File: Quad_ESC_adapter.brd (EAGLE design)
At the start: 96.5 x 40.1 mm, 28 parts, among them Y1 ECS-80-S-4X

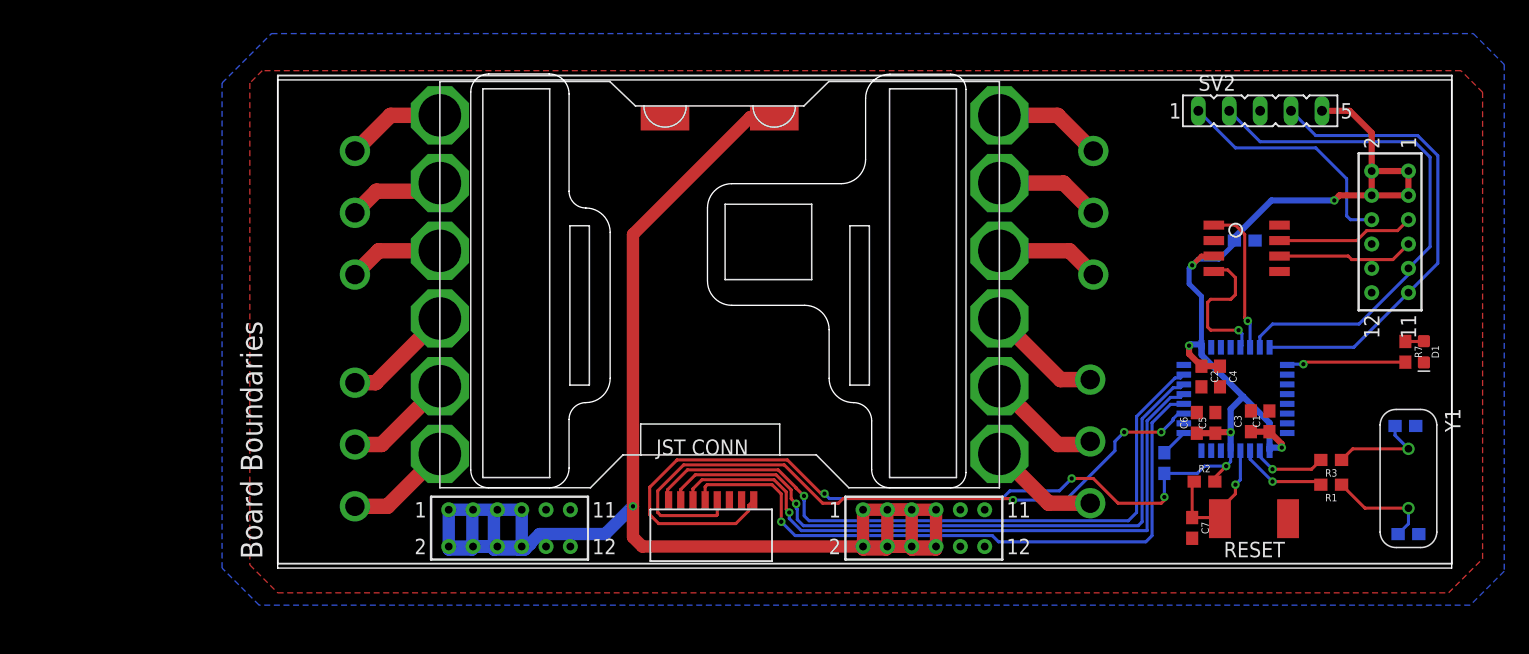
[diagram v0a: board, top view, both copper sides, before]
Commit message: split into adapter board
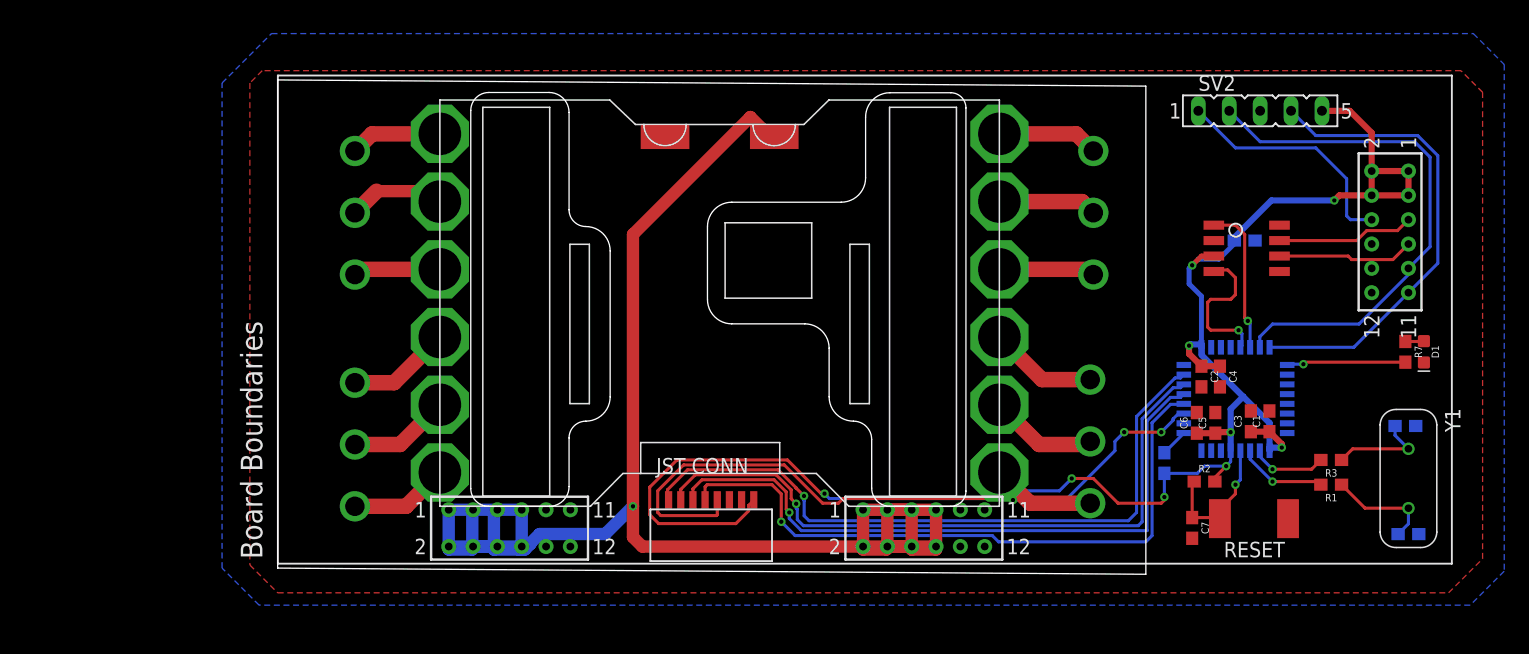
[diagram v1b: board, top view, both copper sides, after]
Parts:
- moved U$10 1.52 mm to (13.3, 5.08)
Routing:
- net ESC4_B: track 9.55 -> 8.92 mm
- net ESC2_B: track 9.17 -> 8.54 mm
- net ESC3_R: track 8.53 -> 7.90 mm
- net ESC2_Y: track 8.97 -> 8.34 mm
- net ESC1_R: track 7.79 -> 7.16 mm
- net ESC4_R: track 9.14 -> 8.51 mm
- net ESC3_Y: track 8.73 -> 8.10 mm
- net ESC2_R: track 8.77 -> 8.14 mm
- net +12V: track 139.0 -> 139.6 mm
- net ESC4_Y: track 9.56 -> 8.93 mm
- net ESC3_B: track 8.94 -> 8.31 mm
- net ESC1_B: track 8.20 -> 7.57 mm
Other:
- board size 96.5 x 40.1 mm -> 71.4 x 40.6 mm
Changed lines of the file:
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@@
 <board>
 <plain>
-<wire x1="0" y1="0" x2="96.52" y2="0" width="0" layer="20"/>
-<wire x1="96.52" y1="0" x2="96.52" y2="40.132" width="0" layer="20"/>
-<wire x1="96.52" y1="40.132" x2="0" y2="40.132" width="0" layer="20"/>
+<wire x1="0" y1="0" x2="71.374" y2="-0.508" width="0" layer="20"/>
+<wire x1="71.374" y1="-0.508" x2="71.374" y2="39.624" width="0" layer="20"/>
+<wire x1="71.374" y1="39.624" x2="0" y2="40.132" width="0" layer="20"/>
 <wire x1="0" y1="40.132" x2="0" y2="0" width="0" layer="20"/>
 </plain>
@@
 <attribute name="VALUE" x="79.44111875" y="25.97543125" size="1.27245" layer="27" rot="R180"/>
 </element>
-<element name="U$10" library="BLHeli_32 45A" package="LUMENIER_QUAD" package3d_urn="urn:adsk.eagle:package:24294694/3" value="LUMENIER_QUAD" x="13.335" y="6.604" smashed="yes"/>
+<element name="U$10" library="BLHeli_32 45A" package="LUMENIER_QUAD" package3d_urn="urn:adsk.eagle:package:24294694/3" value="LUMENIER_QUAD" x="13.335" y="5.08" smashed="yes"/>
 <element name="R4" library="SparkFun-Resistors" library_urn="urn:adsk.eagle:library:532" package="0603" package3d_urn="urn:adsk.eagle:package:39650/1" value="10k" x="72.898" y="8.636" smashed="yes" rot="MR90">
 <attribute name="NAME" x="73.66" y="8.636" size="0.6096" layer="26" font="vector" ratio="20" rot="MR90" align="bottom-center"/>
@@
 <wire x1="52.1244" y1="1.7738" x2="54.1244" y2="1.7738" width="1.016" layer="1"/>
 <wire x1="50.1244" y1="1.7738" x2="52.1244" y2="1.7738" width="1.016" layer="1"/>
-<wire x1="38.862" y1="37.084" x2="38.972" y2="36.974" width="1.016" layer="1"/>
+<wire x1="38.862" y1="37.084" x2="40.496" y2="35.45" width="1.016" layer="1"/>
 <wire x1="38.862" y1="37.084" x2="29.21" y2="27.432" width="1.016" layer="1"/>
-<wire x1="38.972" y1="36.974" x2="40.825" y2="36.974" width="1.016" layer="1"/>
+<wire x1="40.496" y1="35.45" x2="40.825" y2="35.45" width="1.016" layer="1"/>
 <wire x1="50.1244" y1="1.7738" x2="51.8746" y2="1.7738" width="1.016" layer="1"/>
 <wire x1="51.8746" y1="1.7738" x2="52.1244" y2="1.524" width="1.016" layer="1"/>
@@
 <contactref element="U$7" pad="A"/>
 <contactref element="U$10" pad="9"/>
-<wire x1="59.335" y1="20.524" x2="64.365" y2="15.494" width="1.27" layer="1"/>
-<wire x1="64.365" y1="15.494" x2="66.802" y2="15.494" width="1.27" layer="1"/>
+<wire x1="59.335" y1="19" x2="62.841" y2="15.494" width="1.27" layer="1"/>
+<wire x1="62.841" y1="15.494" x2="66.802" y2="15.494" width="1.27" layer="1"/>
 </signal>
 <signal name="ESC4_Y">
 <contactref element="U$7" pad="B"/>
 <contactref element="U$10" pad="8"/>
-<wire x1="59.335" y1="14.954" x2="64.129" y2="10.16" width="1.27" layer="1"/>
-<wire x1="66.294" y1="10.16" x2="64.129" y2="10.16" width="1.27" layer="1"/>
+<wire x1="59.335" y1="13.43" x2="62.605" y2="10.16" width="1.27" layer="1"/>
+<wire x1="66.294" y1="10.16" x2="62.605" y2="10.16" width="1.27" layer="1"/>
 <wire x1="66.802" y1="10.414" x2="66.548" y2="10.16" width="1.016" layer="1"/>
 <wire x1="66.548" y1="10.16" x2="66.294" y2="10.16" width="1.016" layer="1"/>
@@
 <contactref element="U$7" pad="C"/>
 <contactref element="U$10" pad="7"/>
-<wire x1="59.335" y1="9.384" x2="63.385" y2="5.334" width="1.27" layer="1"/>
-<wire x1="63.385" y1="5.334" x2="66.802" y2="5.334" width="1.27" layer="1"/>
+<wire x1="59.335" y1="7.86" x2="61.861" y2="5.334" width="1.27" layer="1"/>
+<wire x1="61.861" y1="5.334" x2="66.802" y2="5.334" width="1.27" layer="1"/>
 </signal>
 <signal name="ESC3_B">
 <contactref element="U$6" pad="A"/>
 <contactref element="U$10" pad="12"/>
-<wire x1="67.056" y1="34.29" x2="64.122" y2="37.224" width="1.27" layer="1"/>
-<wire x1="64.122" y1="37.224" x2="59.335" y2="37.224" width="1.27" layer="1"/>
+<wire x1="67.056" y1="34.29" x2="65.646" y2="35.7" width="1.27" layer="1"/>
+<wire x1="65.646" y1="35.7" x2="59.335" y2="35.7" width="1.27" layer="1"/>
 </signal>
 <signal name="ESC3_Y">
 <contactref element="U$6" pad="B"/>
 <contactref element="U$10" pad="11"/>
-<wire x1="59.335" y1="31.654" x2="64.612" y2="31.654" width="1.27" layer="1"/>
-<wire x1="64.612" y1="31.654" x2="67.056" y2="29.21" width="1.27" layer="1"/>
+<wire x1="59.335" y1="30.13" x2="66.136" y2="30.13" width="1.27" layer="1"/>
+<wire x1="66.136" y1="30.13" x2="67.056" y2="29.21" width="1.27" layer="1"/>
 </signal>
 <signal name="ESC3_R">
 <contactref element="U$6" pad="C"/>
 <contactref element="U$10" pad="10"/>
-<wire x1="59.335" y1="26.084" x2="65.102" y2="26.084" width="1.27" layer="1"/>
-<wire x1="65.102" y1="26.084" x2="67.056" y2="24.13" width="1.27" layer="1"/>
+<wire x1="59.335" y1="24.56" x2="66.626" y2="24.56" width="1.27" layer="1"/>
+<wire x1="66.626" y1="24.56" x2="67.056" y2="24.13" width="1.27" layer="1"/>
 </signal>
 <signal name="ESC2_B">
 <contactref element="U$5" pad="A"/>
 <contactref element="U$10" pad="4"/>
-<wire x1="13.335" y1="20.524" x2="8.051" y2="15.24" width="1.27" layer="1"/>
-<wire x1="8.051" y1="15.24" x2="6.35" y2="15.24" width="1.27" layer="1"/>
+<wire x1="13.335" y1="19" x2="9.575" y2="15.24" width="1.27" layer="1"/>
+<wire x1="9.575" y1="15.24" x2="6.35" y2="15.24" width="1.27" layer="1"/>
 </signal>
 <signal name="ESC2_Y">
 <contactref element="U$5" pad="B"/>
 <contactref element="U$10" pad="5"/>
-<wire x1="13.335" y1="14.954" x2="8.541" y2="10.16" width="1.27" layer="1"/>
-<wire x1="8.541" y1="10.16" x2="6.35" y2="10.16" width="1.27" layer="1"/>
+<wire x1="13.335" y1="13.43" x2="10.065" y2="10.16" width="1.27" layer="1"/>
+<wire x1="10.065" y1="10.16" x2="6.35" y2="10.16" width="1.27" layer="1"/>
 </signal>
 <signal name="ESC2_R">
 <contactref element="U$5" pad="C"/>
 <contactref element="U$10" pad="6"/>
-<wire x1="13.335" y1="9.384" x2="9.031" y2="5.08" width="1.27" layer="1"/>
-<wire x1="9.031" y1="5.08" x2="6.35" y2="5.08" width="1.27" layer="1"/>
+<wire x1="13.335" y1="7.86" x2="10.555" y2="5.08" width="1.27" layer="1"/>
+<wire x1="10.555" y1="5.08" x2="6.35" y2="5.08" width="1.27" layer="1"/>
 </signal>
 <signal name="ESC1_B">
 <contactref element="U$1" pad="A"/>
 <contactref element="U$10" pad="1"/>
-<wire x1="6.35" y1="34.29" x2="9.284" y2="37.224" width="1.27" layer="1"/>
-<wire x1="9.284" y1="37.224" x2="13.335" y2="37.224" width="1.27" layer="1"/>
+<wire x1="6.35" y1="34.29" x2="7.76" y2="35.7" width="1.27" layer="1"/>
+<wire x1="7.76" y1="35.7" x2="13.335" y2="35.7" width="1.27" layer="1"/>
 </signal>
 <signal name="ESC1_Y">
@@
 <contactref element="U$10" pad="2"/>
 <wire x1="6.35" y1="29.21" x2="8.128" y2="30.988" width="1.27" layer="1"/>
-<wire x1="12.954" y1="30.988" x2="8.128" y2="30.988" width="1.27" layer="1"/>
-<wire x1="13.335" y1="31.654" x2="12.954" y2="31.273" width="1.016" layer="1"/>
-<wire x1="12.954" y1="31.273" x2="12.954" y2="30.988" width="1.016" layer="1"/>
+<wire x1="13.335" y1="30.13" x2="12.477" y2="30.988" width="1.016" layer="1"/>
+<wire x1="12.477" y1="30.988" x2="8.128" y2="30.988" width="1.016" layer="1"/>
 </signal>
 <signal name="ESC1_R">
 <contactref element="U$1" pad="C"/>
 <contactref element="U$10" pad="3"/>
-<wire x1="6.35" y1="24.13" x2="8.304" y2="26.084" width="1.27" layer="1"/>
-<wire x1="8.304" y1="26.084" x2="13.335" y2="26.084" width="1.27" layer="1"/>
+<wire x1="6.35" y1="24.13" x2="6.78" y2="24.56" width="1.27" layer="1"/>
+<wire x1="6.78" y1="24.56" x2="13.335" y2="24.56" width="1.27" layer="1"/>
 </signal>
 <signal name="CAN_H">

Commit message: complete connector placement
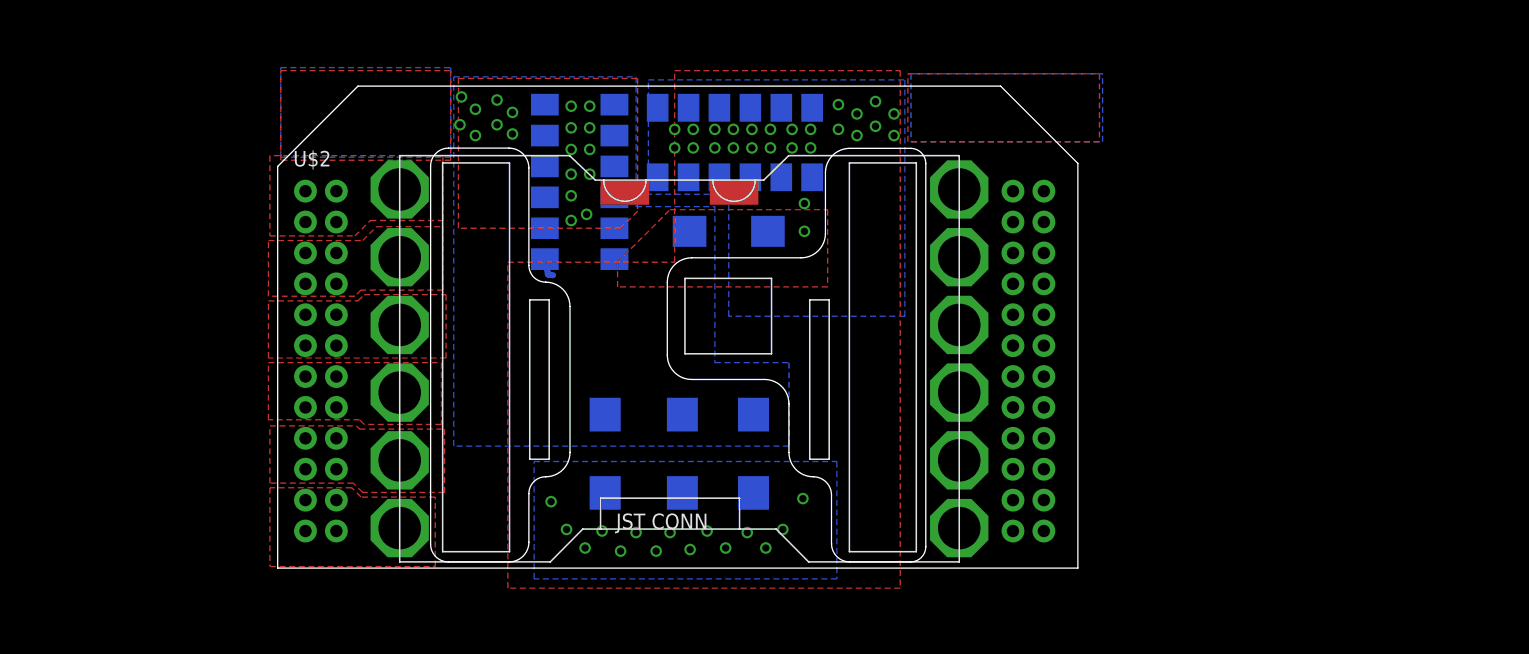
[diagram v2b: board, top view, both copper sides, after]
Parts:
- removed C10: 100nF, SparkFun-Capacitors:0603
- removed C5, C6, C7, C8, C9: 4.7uF, SparkFun-Capacitors:0603
- removed D1: (no value), SparkFun-LED:LED-0603
- removed R1, R2, R3: 1k, SparkFun-Resistors:0603
- removed R4: 10k, SparkFun-Resistors:0603
- removed R7: (no value), SparkFun-Resistors:0603
- removed RESET: (no value), DiscreteComponents:SW_2512
- removed SV2: (no value), con-lsta:FE05-1
- removed U$1, U$5, U$6, U$7: 3PINCONNECTOR, BLHeli_32 45A:3PINCONNECTOR
- removed U$3: BACKPLANE_CONNECTORS, BLHeli_32 45A:BACKPLANE_CONNECTORS
- removed U$4: STM32F042K6T6, PI_Shield_Library:STM32F042K6T6
- removed U$8: TCAN337D, PI_Shield_Library:TCAN337D
- removed Y1: ECS-80-S-4X, ECS-80-S-4X:XTAL_ECS-80-S-4X
- C1, C2, C3, C4: value 4.7uF -> 150uF; device SparkFun-Capacitors:0603 -> Tantalum Cap 150 uF - Kemet 2917 T491:2917(7343-31-METRIC)
- U$2: value 8PIN_CONNECTOR -> BACKPLANE_ESC_ADAPTER_ESC; device BLHeli_32 45A:8PI_CONNECTOR -> Backplane_ESC_adapter:BACKPLANE_ESC_ADAPTER_ESC
- moved C1 54.7 mm to (26.9, 9.40), flipped to the bottom
- moved C2 43.1 mm to (33.3, 9.40), flipped to the bottom, turned to 90 degrees
- moved C4 42.1 mm to (37.1, 27.7), flipped to the bottom, turned to 0 degrees
- moved C3 41.0 mm to (39.1, 9.40), flipped to the bottom
- moved U$2 40.9 mm to (0.00, 0.00), turned to 0 degrees
- moved U$10 5.64 mm to (10.0, 0.51)
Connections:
- removed net +12V: U$10.VIN, U$3.1, U$3.13, U$3.14, U$3.15, U$3.16, U$3.17, U$3.18, U$3.19, U$3.2, U$3.20, U$3.3, U$3.4, U$3.5, U$3.6, U$3.7, U$3.8
- removed net +3V3: C1.1, C10.1, C2.1, C3.1, C4.1, C5.1, C6.1, R2.2, R4.1, SV2.5, U$2.P$1, U$3.25, U$3.26, U$3.27, U$3.28, U$4.VDD, U$4.VDDA, U$4.VDDIO2, U$8.VCC
- removed net CAN_H: U$3.29, U$8.CANH
- removed net CAN_L: U$3.31, U$8.CANL
- removed net CAN_RX: U$4.PA11, U$8.RXD
- removed net CAN_TX: U$4.PA12, U$8.TXD
- removed net LED: R7.2, U$4.PA15
- removed net N$1: C9.1, R1.1, Y1.2
- removed net N$2: C8.1, R3.1, Y1.1
- removed net N$24: D1.A, R7.1
- removed net N$3: R4.2, U$4.PA3
- removed net N$7: U$3.32
- removed net N$8: U$3.36
- removed net NRST: SV2.1, U$3.30
- removed net NRST1: C7.1, R2.1, RESET.2, U$4.NRST
- removed net OSC_IN: R3.2, U$4.PF0-OSC_IN
- removed net OSC_OUT: R1.2, U$4.PF1-OSC_OUT
- removed net SWCLK: SV2.4, U$3.35, U$4.PA14
- removed net SWDIO: SV2.2, U$3.33, U$4.PA13
- removed net TIM3_CH1: U$2.P$5, U$4.PA6
- removed net TIM3_CH2: U$2.P$6, U$4.PA7
- removed net TIM3_CH3: U$2.P$7, U$4.PB0
- removed net TIM3_CH4: U$2.P$8, U$4.PB1
- removed net TLM: U$2.P$4, U$4.PA5
- new net 12V: C1.+, C2.+, C3.+, C4.+, U$10.VIN, U$2.12V@1, U$2.12V@10, U$2.12V@11, U$2.12V@12, U$2.12V@2, U$2.12V@3, U$2.12V@4, U$2.12V@5, U$2.12V@6, U$2.12V@7, U$2.12V@8, U$2.12V@9
- net ESC1_B: now also U$2.ESC1_P1@1, U$2.ESC1_P1@2, U$2.ESC1_P1@3, U$2.ESC1_P1@4; no longer U$1.A
- net ESC1_R: now also U$2.ESC1_P3@1, U$2.ESC1_P3@2, U$2.ESC1_P3@3, U$2.ESC1_P3@4; no longer U$1.C
- net ESC1_Y: now also U$2.ESC1_P2@1, U$2.ESC1_P2@2, U$2.ESC1_P2@3, U$2.ESC1_P2@4; no longer U$1.B
- net ESC2_B: now also U$2.ESC2_P1@1, U$2.ESC2_P1@2, U$2.ESC2_P1@3, U$2.ESC2_P1@4; no longer U$5.A
- net ESC2_R: now also U$2.ESC2_P3@1, U$2.ESC2_P3@2, U$2.ESC2_P3@3, U$2.ESC2_P3@4; no longer U$5.C
- net ESC2_Y: now also U$2.ESC2_P2@1, U$2.ESC2_P2@2, U$2.ESC2_P2@3, U$2.ESC2_P2@4; no longer U$5.B
- net ESC3_B: now also U$2.ESC3_P1@1, U$2.ESC3_P1@2, U$2.ESC3_P1@3, U$2.ESC3_P1@4; no longer U$6.A
- net ESC3_R: now also U$2.ESC3_P3@1, U$2.ESC3_P3@2, U$2.ESC3_P3@3, U$2.ESC3_P3@4; no longer U$6.C
- net ESC3_Y: now also U$2.ESC3_P2@1, U$2.ESC3_P2@2, U$2.ESC3_P2@3, U$2.ESC3_P2@4; no longer U$6.B
- net ESC4_B: now also U$2.ESC4_P1@1, U$2.ESC4_P1@2, U$2.ESC4_P1@3, U$2.ESC4_P1@4; no longer U$7.A
- net ESC4_R: now also U$2.ESC4_P3@1, U$2.ESC4_P3@2, U$2.ESC4_P3@3, U$2.ESC4_P3@4; no longer U$7.C
- net ESC4_Y: now also U$2.ESC4_P2@1, U$2.ESC4_P2@2, U$2.ESC4_P2@3, U$2.ESC4_P2@4; no longer U$7.B
- net GND: now also C1.-, C2.-, C3.-, C4.-, U$2.GND@1, U$2.GND@10, U$2.GND@11, U$2.GND@12, U$2.GND@2, U$2.GND@3, U$2.GND@4, U$2.GND@5, U$2.GND@6, U$2.GND@7, U$2.GND@8, U$2.GND@9; no longer C1.2, C10.2, C2.2, C3.2, C4.2, C5.2, C6.2, C7.2, C8.2, C9.2, D1.C, RESET.1, SV2.3, U$2.P$2, U$2.P$3, U$3.10, U$3.11, U$3.12, U$3.21, U$3.22, U$3.23, U$3.24, U$3.9, U$4.PB8-BOOT0, U$4.VSS, U$4.VSS1, U$8.GND
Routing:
- net +3V3: track 141.8 -> 0.00 mm, vias 9 -> 0
- net +12V: track 139.6 -> 0.00 mm, vias 1 -> 0
- net TLM: track 57.1 -> 0.00 mm, vias 3 -> 0
- net TIM3_CH4: track 56.3 -> 0.00 mm, vias 1 -> 0
- net TIM3_CH3: track 55.4 -> 0.00 mm, vias 1 -> 0
- net TIM3_CH2: track 54.4 -> 0.00 mm, vias 1 -> 0
- net TIM3_CH1: track 54.0 -> 0.00 mm, vias 1 -> 0
- net SWDIO: track 43.7 -> 0.00 mm
- net SWCLK: track 39.1 -> 0.00 mm
- net NRST: track 19.7 -> 0.00 mm
- net NRST1: track 12.6 -> 0.00 mm, vias 1 -> 0
- net CAN_TX: track 12.3 -> 0.00 mm, vias 1 -> 0
- net CAN_RX: track 12.3 -> 0.00 mm, vias 1 -> 0
- net CAN_H: track 11.3 -> 0.00 mm
- net CAN_L: track 11.3 -> 0.00 mm
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- added copper zone on layer 1, net 12V
- added copper zone on layer 16, net 12V
- added copper zone on layer 1, net ESC1_B
- added copper zone on layer 1, net ESC1_R
- added copper zone on layer 1, net ESC1_Y
- added copper zone on layer 1, net ESC2_B
- added copper zone on layer 1, net ESC2_R
- added copper zone on layer 1, net ESC2_Y
- added copper zone on layer 1, net FILL_B_L
- added copper zone on layer 16, net FILL_B_L
- added copper zone on layer 1, net FILL_B_R
- added copper zone on layer 16, net FILL_B_R
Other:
- board size 71.4 x 40.6 mm -> 65.8 x 39.6 mm

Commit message: tented vias under lumenier
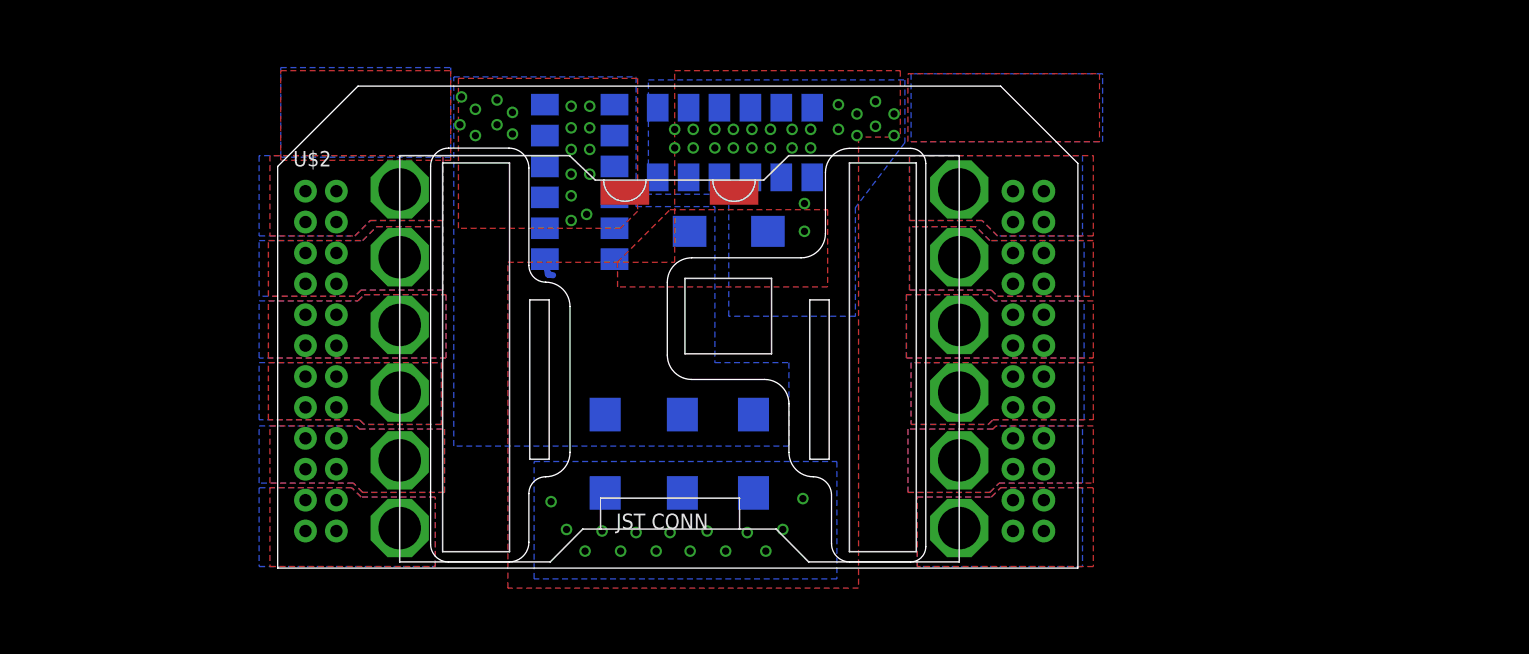
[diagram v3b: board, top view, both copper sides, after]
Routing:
- added copper zone on layer 16, net ESC1_B
- added copper zone on layer 16, net ESC1_R
- added copper zone on layer 16, net ESC1_Y
- added copper zone on layer 16, net ESC2_B
- added copper zone on layer 16, net ESC2_R
- added copper zone on layer 16, net ESC2_Y
- added copper zone on layer 1, net ESC3_B
- added copper zone on layer 16, net ESC3_B
- added copper zone on layer 1, net ESC3_R
- added copper zone on layer 16, net ESC3_R
- added copper zone on layer 1, net ESC3_Y
- added copper zone on layer 16, net ESC3_Y
- added copper zone on layer 1, net ESC4_B
- added copper zone on layer 16, net ESC4_B
- added copper zone on layer 1, net ESC4_R
- added copper zone on layer 16, net ESC4_R
- added copper zone on layer 1, net ESC4_Y
- added copper zone on layer 16, net ESC4_Y
